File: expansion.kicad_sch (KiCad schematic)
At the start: 8 parts, among them J4 PMOD_A, J5 PMOD_B, J6 MEZZANINE

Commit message: schematic wip
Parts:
- removed J5: PMOD_B, mainboard:PinSocket_2x06_P2.54mm_PMOD, symbol Connector_Generic:Conn_02x06_Top_Bottom
- removed RN6, RN7: 33, Resistor_SMD:R_Array_Convex_4x0402, symbol Device:R_Pack04
- C52: Part Number CL05A105MQ5NNNC -> CL05A105KP5NNNC; Substitution CL05A105KQ5NNNC, CL05A105KP5NNNC, CL05A105KO5NNNC -> any equivalent
- J4: value PMOD_A -> PMOD
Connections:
- net A0 renamed P1
- net A1 renamed P2
- net A2 renamed P3
- net A3 renamed P4
- net A4 renamed P7
- net A5 renamed P8
- net A6 renamed P9
- net A7 renamed P10
- net PMOD_A0 renamed PMOD1
- net PMOD_A1 renamed PMOD2
- net PMOD_A2 renamed PMOD3
- net PMOD_A3 renamed PMOD4
- net PMOD_A4 renamed PMOD7
- net PMOD_A5 renamed PMOD8
- net PMOD_A6 renamed PMOD9
- net PMOD_A7 renamed PMOD10
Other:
- moved on the sheet: RN4, RN5

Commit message: update symbol metadata
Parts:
- J4: Note populate only when assembling for installation in enclosure -> (none)
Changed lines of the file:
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@@
-      (effects (font (size 1.27 1.27)) hide)
-    )
-    (property "Note" "populate only when assembling for installation in enclosure" (at 104.14 87.63 0)
       (effects (font (size 1.27 1.27)) hide)
     )

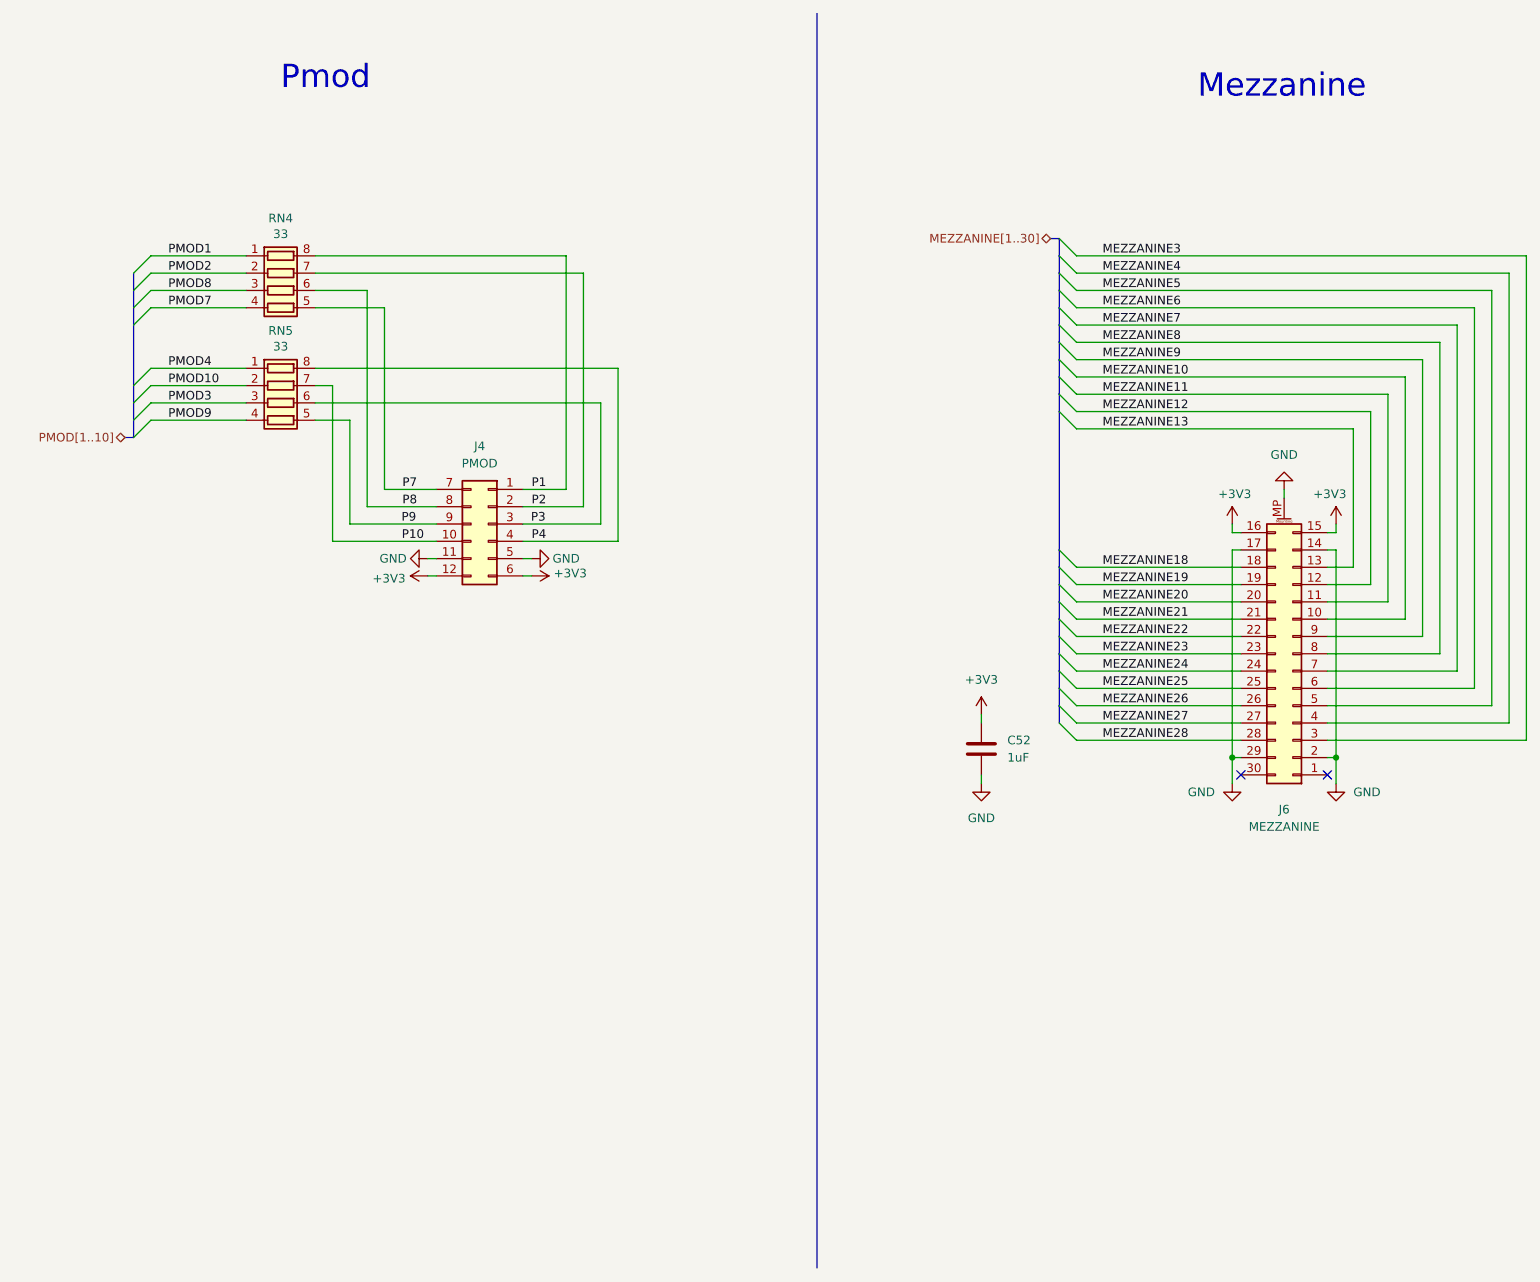
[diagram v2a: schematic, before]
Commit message: complete initial layout
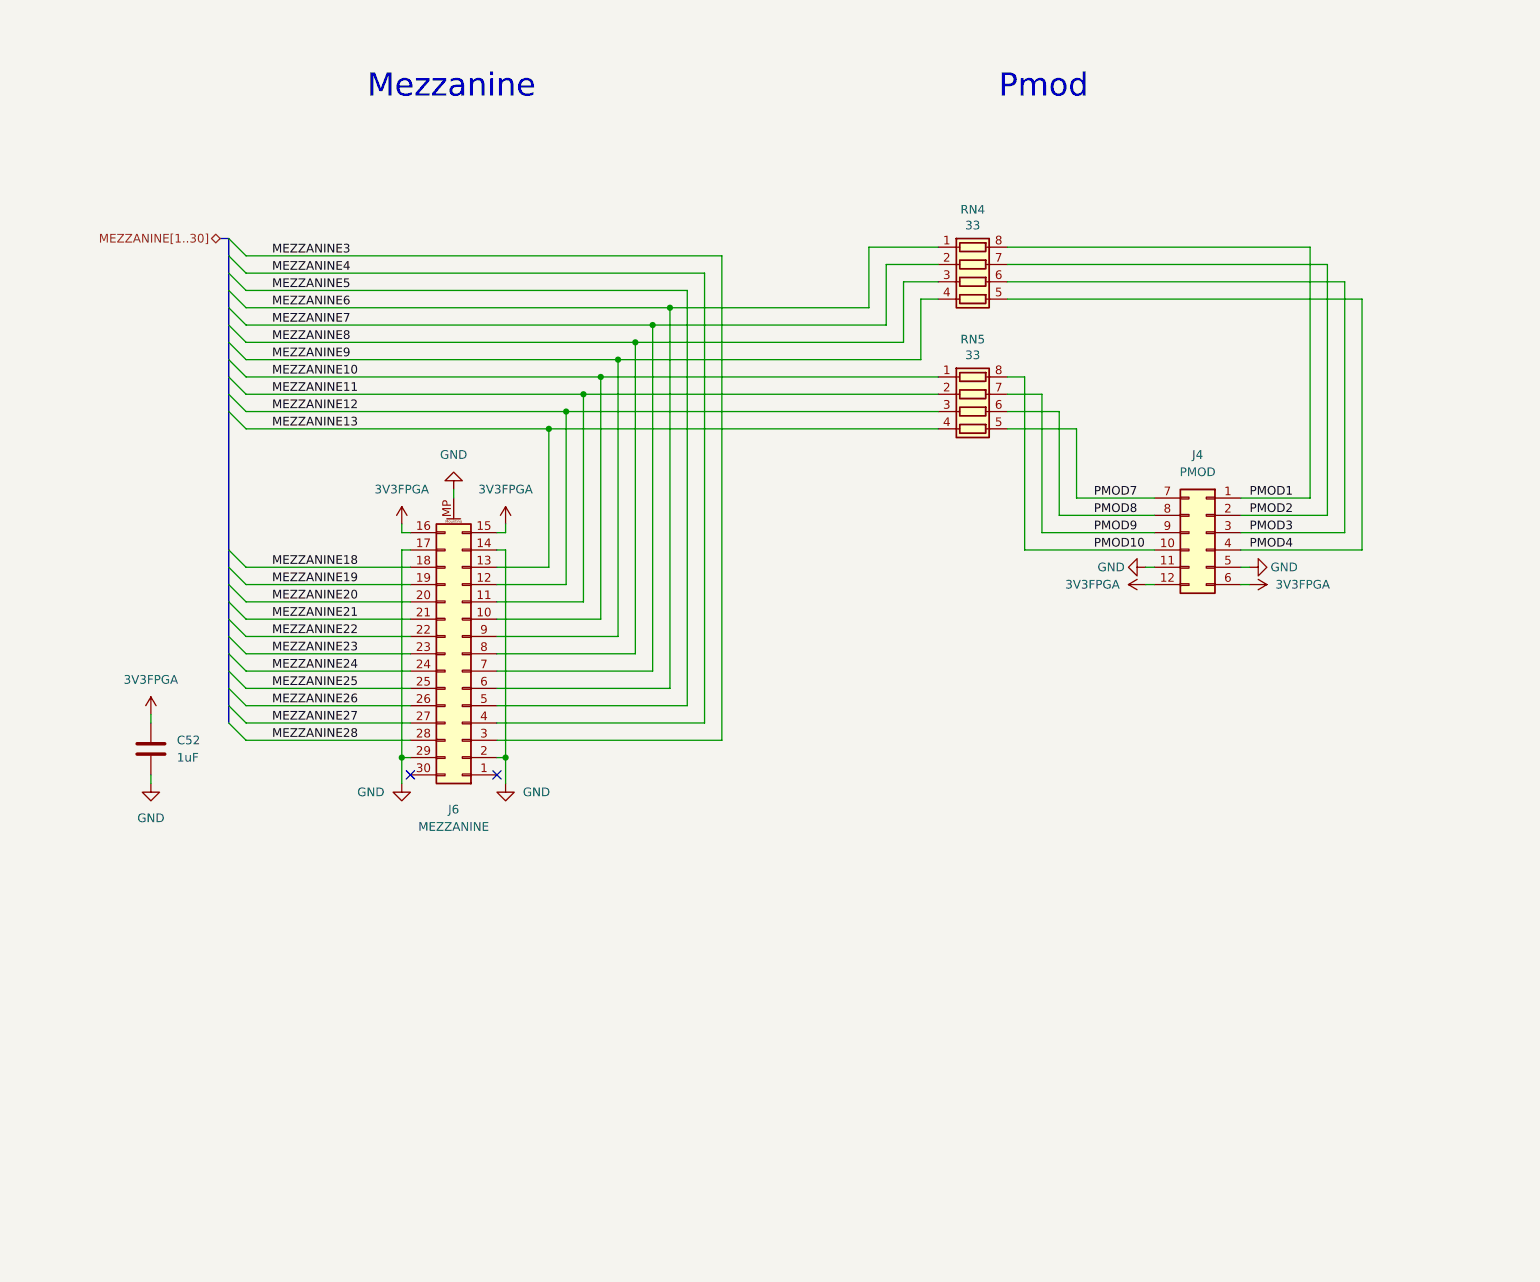
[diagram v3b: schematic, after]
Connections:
- net P1 is gone; now on net PMOD1: J4.1 (Pin_1), RN4.8 (R1.2)
- net P2 is gone; now on net PMOD2: J4.2 (Pin_2), RN4.7 (R2.2)
- net MEZZANINE10: now also RN5.1 (R1.1)
- net MEZZANINE11: now also RN5.2 (R2.1)
- net MEZZANINE12: now also RN5.3 (R3.1)
- net MEZZANINE13: now also RN5.4 (R4.1)
- net MEZZANINE6: now also RN4.1 (R1.1)
- net MEZZANINE7: now also RN4.2 (R2.1)
- net MEZZANINE8: now also RN4.3 (R3.1)
- net MEZZANINE9: now also RN4.4 (R4.1)
- net PMOD1: no longer RN4.1 (R1.1)
- net PMOD10: now also J4.10 (Pin_10), RN5.8 (R1.2); no longer RN5.2 (R2.1)
- net PMOD2: no longer RN4.2 (R2.1)
- net PMOD3: now also J4.3 (Pin_3), RN4.6 (R3.2); no longer RN5.3 (R3.1)
- net PMOD4: now also J4.4 (Pin_4), RN4.5 (R4.2); no longer RN5.1 (R1.1)
- net PMOD7: now also J4.7 (Pin_7), RN5.5 (R4.2); no longer RN4.4 (R4.1)
- net PMOD8: now also J4.8 (Pin_8), RN5.6 (R3.2); no longer RN4.3 (R3.1)
- net PMOD9: now also J4.9 (Pin_9), RN5.7 (R2.2); no longer RN5.4 (R4.1)
- net +3V3 renamed 3V3FPGA
- removed net P10: J4.10 (Pin_10), RN5.7 (R2.2)
- removed net P3: J4.3 (Pin_3), RN5.6 (R3.2)
- removed net P4: J4.4 (Pin_4), RN5.8 (R1.2)
- removed net P7: J4.7 (Pin_7), RN4.5 (R4.2)
- removed net P8: J4.8 (Pin_8), RN4.6 (R3.2)
- removed net P9: J4.9 (Pin_9), RN5.5 (R4.2)
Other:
- moved on the sheet: C52, J4, J6, RN4, RN5
